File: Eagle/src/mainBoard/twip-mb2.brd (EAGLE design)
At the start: 82.2 x 82.5 mm, 19 parts, among them U1 GY-521MPU6050

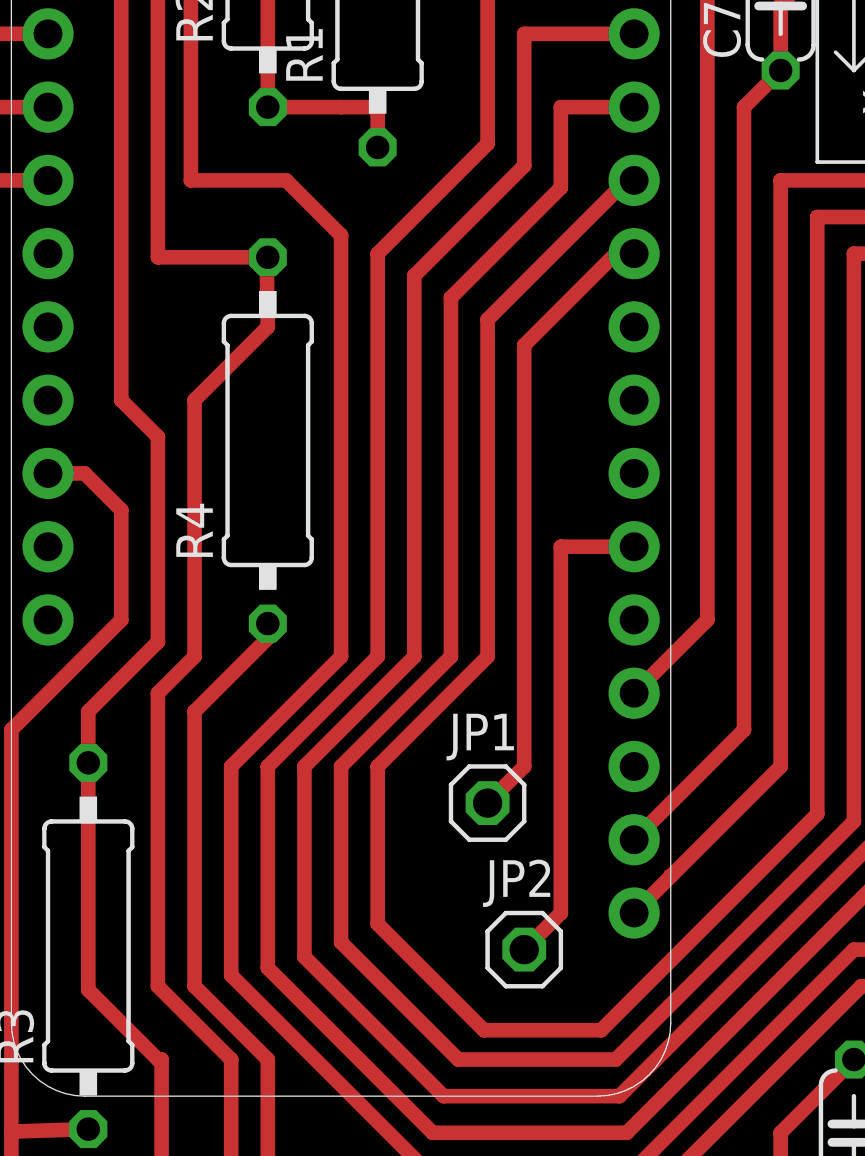
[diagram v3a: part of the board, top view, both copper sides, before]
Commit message: Update twip-mb2.brd
 mosfet pullup changes
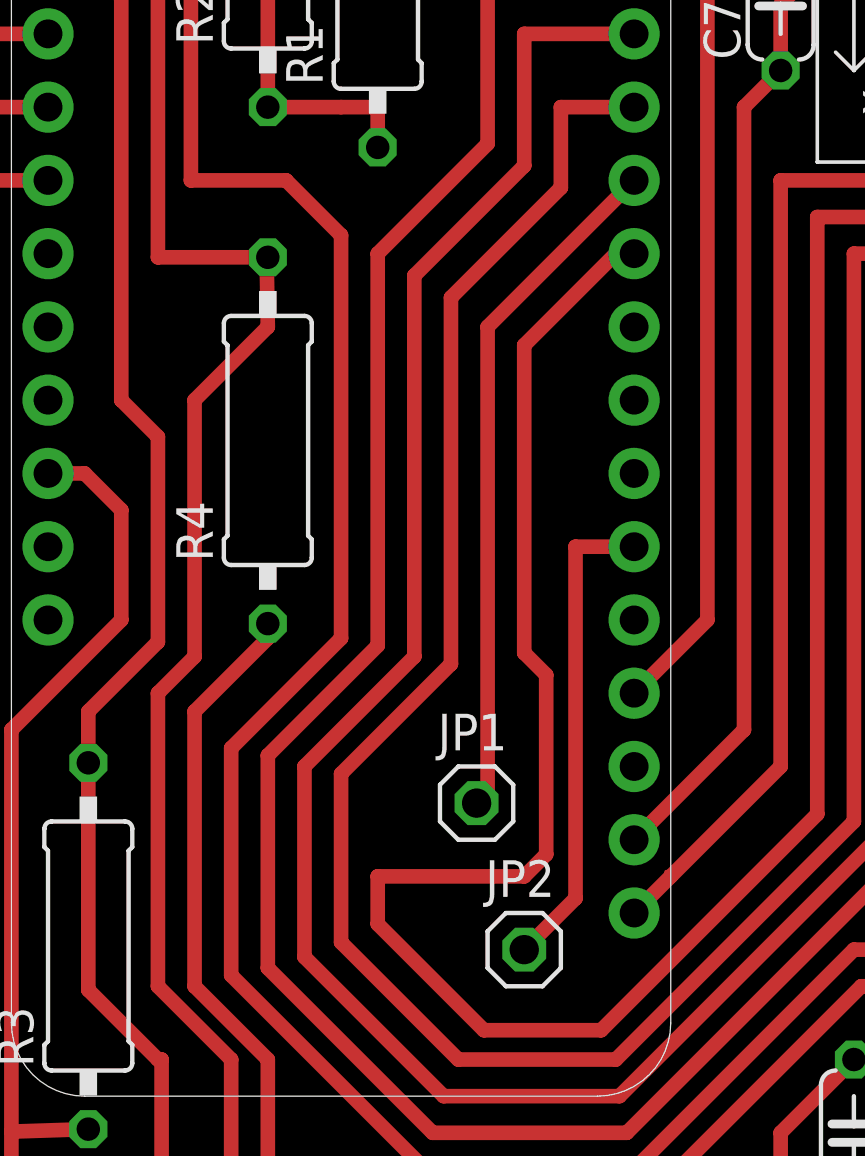
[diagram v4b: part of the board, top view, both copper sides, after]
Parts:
- moved JP1 0.38 mm to (25.0, 39.4)
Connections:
- net N$31: now also STEPDRV1.1; no longer JP1.1
- net N$32: now also JP1.1; no longer STEPDRV1.1
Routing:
- net N$31: track 21.5 -> 158.8 mm
- net N$32: track 157.5 -> 23.9 mm
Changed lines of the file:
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@@
 <attribute name="VALUE" x="64.897" y="68.961" size="1.27" layer="27" ratio="10" rot="R90"/>
 </element>
-<element name="JP1" library="pinhead" library_urn="urn:adsk.eagle:library:325" package="1X01" package3d_urn="urn:adsk.eagle:package:22485/2" value="" x="25.4" y="39.37" smashed="yes">
-<attribute name="NAME" x="24.0538" y="41.1988" size="1.27" layer="25" ratio="10"/>
-<attribute name="VALUE" x="24.13" y="36.195" size="1.27" layer="27"/>
+<element name="JP1" library="pinhead" library_urn="urn:adsk.eagle:library:325" package="1X01" package3d_urn="urn:adsk.eagle:package:22485/2" value="" x="25.019" y="39.37" smashed="yes">
+<attribute name="NAME" x="23.6728" y="41.1988" size="1.27" layer="25" ratio="10"/>
+<attribute name="VALUE" x="23.749" y="36.195" size="1.27" layer="27"/>
 </element>
 <element name="JP2" library="pinhead" library_urn="urn:adsk.eagle:library:325" package="1X01" package3d_urn="urn:adsk.eagle:package:22485/2" value="" x="26.67" y="34.29" smashed="yes">
@@
 <wire x1="20.32" y1="34.544" x2="24.384" y2="30.48" width="0.508" layer="1"/>
 <wire x1="74.93" y1="48.26" x2="64.77" y2="58.42" width="0.508" layer="1"/>
-<wire x1="20.32" y1="40.64" x2="20.32" y2="34.544" width="0.508" layer="1"/>
-<wire x1="20.32" y1="40.64" x2="24.13" y2="44.45" width="0.508" layer="1"/>
+<wire x1="20.32" y1="40.386" x2="20.32" y2="34.544" width="0.508" layer="1"/>
+<wire x1="20.32" y1="40.386" x2="24.13" y2="44.196" width="0.508" layer="1"/>
 <wire x1="24.384" y1="30.48" x2="29.845" y2="30.48" width="0.508" layer="1"/>
 <wire x1="29.845" y1="30.48" x2="38.1" y2="38.735" width="0.508" layer="1"/>
-<wire x1="24.13" y1="44.45" x2="24.13" y2="56.896" width="0.508" layer="1"/>
+<wire x1="24.13" y1="44.196" x2="24.13" y2="56.896" width="0.508" layer="1"/>
 <wire x1="27.94" y1="63.5" x2="30.48" y2="63.5" width="0.508" layer="1"/>
 <wire x1="24.13" y1="56.896" x2="27.94" y2="60.706" width="0.508" layer="1"/>
@@
 <wire x1="16.51" y1="33.401" x2="23.241" y2="26.67" width="0.508" layer="1"/>
 <wire x1="30.48" y1="26.67" x2="23.241" y2="26.67" width="0.508" layer="1"/>
-<wire x1="16.51" y1="40.64" x2="20.32" y2="44.45" width="0.508" layer="1"/>
-<wire x1="16.51" y1="40.64" x2="16.51" y2="33.401" width="0.508" layer="1"/>
-<wire x1="20.32" y1="44.45" x2="20.32" y2="59.055" width="0.508" layer="1"/>
+<wire x1="16.51" y1="41.275" x2="20.32" y2="45.085" width="0.508" layer="1"/>
+<wire x1="16.51" y1="41.275" x2="16.51" y2="33.401" width="0.508" layer="1"/>
+<wire x1="20.32" y1="45.085" x2="20.32" y2="59.055" width="0.508" layer="1"/>
 <wire x1="43.2562" y1="34.29" x2="44.2976" y2="33.2486" width="0.508" layer="1"/>
 <wire x1="38.1" y1="34.29" x2="43.2562" y2="34.29" width="0.508" layer="1"/>
@@
 <wire x1="33.02" y1="5.08" x2="30.48" y2="7.62" width="0.508" layer="1"/>
 </signal>
-<signal name="N$32">
-<contactref element="STEPDRV1" pad="1"/>
-<contactref element="MS2" pad="11"/>
-<wire x1="72.39" y1="8.89" x2="74.93" y2="8.89" width="0.508" layer="1"/>
-<wire x1="74.93" y1="8.89" x2="76.2" y2="10.16" width="0.508" layer="1"/>
-<wire x1="76.2" y1="10.16" x2="76.2" y2="49.53" width="0.508" layer="1"/>
-<wire x1="76.2" y1="49.53" x2="66.04" y2="59.69" width="0.508" layer="1"/>
-<wire x1="36.83" y1="59.69" x2="36.83" y2="38.989" width="0.508" layer="1"/>
-<wire x1="36.83" y1="38.989" x2="29.337" y2="31.496" width="0.508" layer="1"/>
-<wire x1="66.04" y1="59.69" x2="36.83" y2="59.69" width="0.508" layer="1"/>
-<wire x1="25.273" y1="31.496" x2="21.59" y2="35.179" width="0.508" layer="1"/>
-<wire x1="21.59" y1="35.179" x2="21.59" y2="40.64" width="0.508" layer="1"/>
-<wire x1="21.59" y1="40.64" x2="25.4" y2="44.45" width="0.508" layer="1"/>
-<wire x1="29.337" y1="31.496" x2="25.273" y2="31.496" width="0.508" layer="1"/>
-<wire x1="25.4" y1="44.45" x2="25.4" y2="56.134" width="0.508" layer="1"/>
-<wire x1="25.4" y1="56.134" x2="30.226" y2="60.96" width="0.508" layer="1"/>
-<wire x1="30.226" y1="60.96" x2="30.48" y2="60.96" width="0.508" layer="1"/>
-</signal>
 <signal name="N$34">
 <contactref element="STEPDRV2" pad="1"/>
@@
 <wire x1="30.226" y1="27.94" x2="23.495" y2="27.94" width="0.508" layer="1"/>
 <wire x1="23.495" y1="27.94" x2="17.78" y2="33.655" width="0.508" layer="1"/>
-<wire x1="17.78" y1="33.655" x2="17.78" y2="40.64" width="0.508" layer="1"/>
-<wire x1="21.59" y1="44.45" x2="17.78" y2="40.64" width="0.508" layer="1"/>
+<wire x1="17.78" y1="33.655" x2="17.78" y2="41.021" width="0.508" layer="1"/>
+<wire x1="21.59" y1="44.831" x2="17.78" y2="41.021" width="0.508" layer="1"/>
 <wire x1="25.4" y1="62.23" x2="25.4" y2="68.58" width="0.508" layer="1"/>
 <wire x1="25.4" y1="68.58" x2="30.48" y2="68.58" width="0.508" layer="1"/>
-<wire x1="21.59" y1="44.45" x2="21.59" y2="58.42" width="0.508" layer="1"/>
+<wire x1="21.59" y1="44.831" x2="21.59" y2="58.42" width="0.508" layer="1"/>
 <wire x1="25.4" y1="62.23" x2="21.59" y2="58.42" width="0.508" layer="1"/>
 <contactref element="IBC" pad="25"/>
@@
 <contactref element="MS2" pad="6"/>
 <contactref element="JP2" pad="1"/>
-<wire x1="30.48" y1="48.26" x2="27.94" y2="48.26" width="0.508" layer="1"/>
-<wire x1="27.94" y1="48.26" x2="27.94" y2="35.56" width="0.508" layer="1"/>
-<wire x1="27.94" y1="35.56" x2="26.67" y2="34.29" width="0.508" layer="1"/>
+<wire x1="30.48" y1="48.26" x2="28.448" y2="48.26" width="0.508" layer="1"/>
+<wire x1="28.448" y1="48.26" x2="28.448" y2="36.068" width="0.508" layer="1"/>
+<wire x1="28.448" y1="36.068" x2="26.67" y2="34.29" width="0.508" layer="1"/>
 </signal>
 <signal name="N$31">
 <contactref element="MS2" pad="10"/>
-<contactref element="JP1" pad="1"/>
-<wire x1="25.4" y1="39.37" x2="26.67" y2="40.64" width="0.508" layer="1"/>
-<wire x1="26.67" y1="40.64" x2="26.67" y2="55.245" width="0.508" layer="1"/>
+<wire x1="26.67" y1="44.577" x2="26.67" y2="55.245" width="0.508" layer="1"/>
 <wire x1="26.67" y1="55.245" x2="29.845" y2="58.42" width="0.508" layer="1"/>
 <wire x1="29.845" y1="58.42" x2="30.48" y2="58.42" width="0.508" layer="1"/>
+<contactref element="STEPDRV1" pad="1"/>
+<wire x1="72.39" y1="8.89" x2="74.93" y2="8.89" width="0.508" layer="1"/>
+<wire x1="74.93" y1="8.89" x2="76.2" y2="10.16" width="0.508" layer="1"/>
+<wire x1="76.2" y1="10.16" x2="76.2" y2="49.53" width="0.508" layer="1"/>
+<wire x1="76.2" y1="49.53" x2="66.04" y2="59.69" width="0.508" layer="1"/>
+<wire x1="36.83" y1="59.69" x2="36.83" y2="38.989" width="0.508" layer="1"/>
+<wire x1="36.83" y1="38.989" x2="29.337" y2="31.496" width="0.508" layer="1"/>
+<wire x1="66.04" y1="59.69" x2="36.83" y2="59.69" width="0.508" layer="1"/>
+<wire x1="25.273" y1="31.496" x2="21.59" y2="35.179" width="0.508" layer="1"/>
+<wire x1="21.59" y1="35.179" x2="21.59" y2="36.83" width="0.508" layer="1"/>
+<wire x1="29.337" y1="31.496" x2="25.273" y2="31.496" width="0.508" layer="1"/>
+<wire x1="26.67" y1="44.577" x2="27.432" y2="43.815" width="0.508" layer="1"/>
+<wire x1="27.432" y1="43.815" x2="27.432" y2="37.592" width="0.508" layer="1"/>
+<wire x1="27.432" y1="37.592" x2="26.67" y2="36.83" width="0.508" layer="1"/>
+<wire x1="26.67" y1="36.83" x2="21.59" y2="36.83" width="0.508" layer="1"/>
 </signal>
 <signal name="N$37">
@@
 <wire x1="54.864" y1="44.704" x2="57.15" y2="46.99" width="0.508" layer="1"/>
 </signal>
+<signal name="N$32">
+<contactref element="MS2" pad="11"/>
+<contactref element="JP1" pad="1"/>
+<wire x1="30.48" y1="60.96" x2="25.4" y2="55.88" width="0.508" layer="1"/>
+<wire x1="25.4" y1="39.751" x2="25.019" y2="39.37" width="0.508" layer="1"/>
+<wire x1="25.4" y1="55.88" x2="25.4" y2="39.751" width="0.508" layer="1"/>
+</signal>
 </signals>

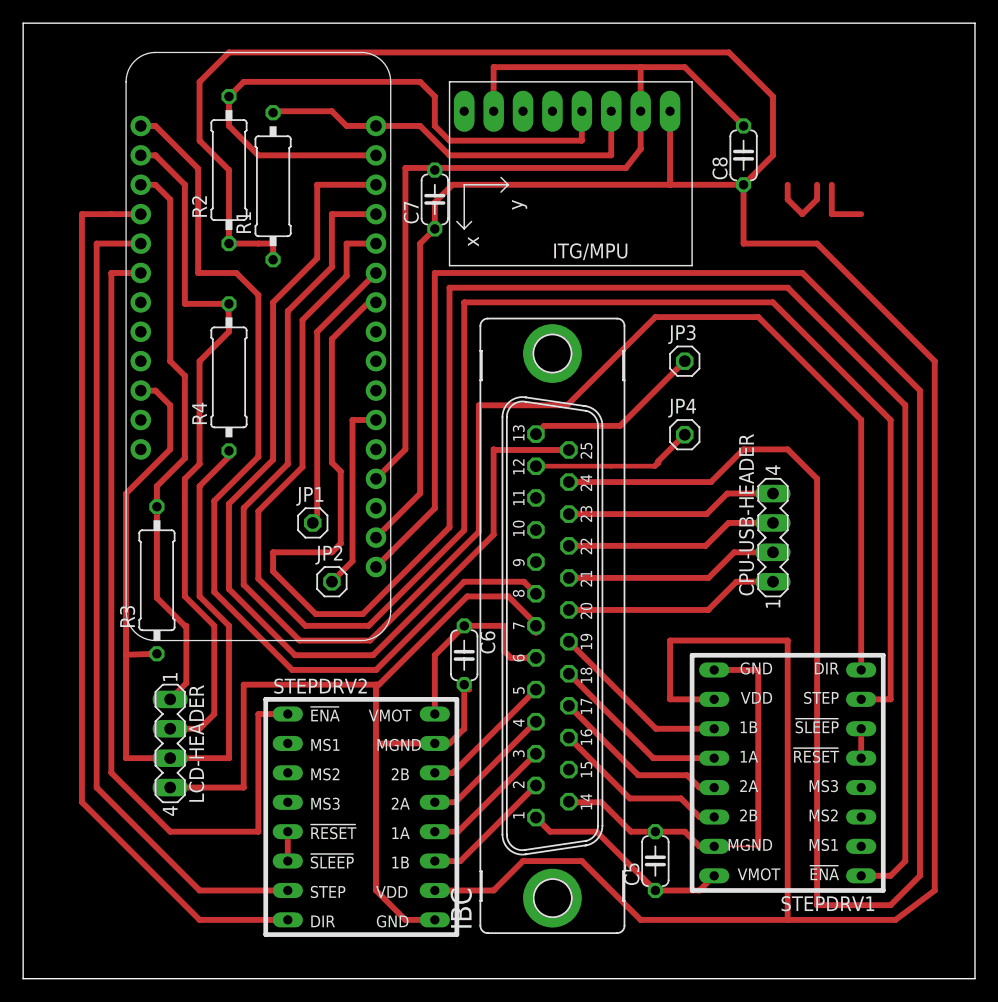
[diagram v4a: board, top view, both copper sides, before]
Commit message: Update twip-mb2.brd
big changes to  IBC pinouts  to  shift stepper connectors around
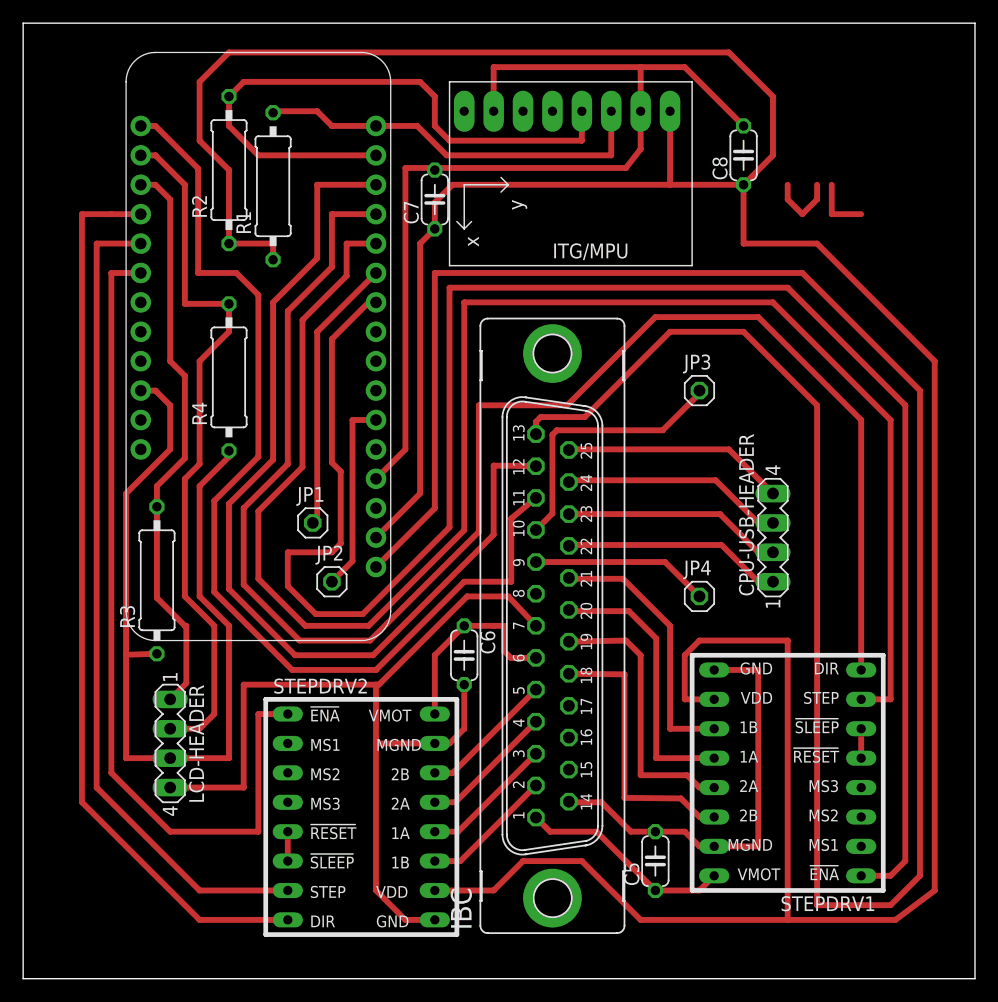
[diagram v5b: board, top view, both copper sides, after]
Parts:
- moved JP4 14.0 mm to (58.4, 33.0)
- moved JP3 2.84 mm to (58.4, 50.8)
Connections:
- net N$13: now also IBC.25; no longer IBC.23
- net N$14: now also IBC.24; no longer IBC.22
- net N$16: now also IBC.13; no longer IBC.24
- net N$18: now also IBC.23; no longer IBC.21
- net N$19: now also IBC.12; no longer IBC.25
- net N$28: now also IBC.11; no longer IBC.8
- net N$3: now also IBC.18; no longer IBC.16
- net N$30: now also IBC.22; no longer IBC.20
- net N$37: now also IBC.10; no longer IBC.13
- net N$38: now also IBC.9; no longer IBC.12
- net N$4: now also IBC.19; no longer IBC.17
- net N$6: now also IBC.20; no longer IBC.18
- net N$7: now also IBC.21; no longer IBC.19
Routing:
- net N$16: track 186.2 -> 199.9 mm
- net N$3: track 15.4 -> 23.9 mm
- net N$4: track 15.5 -> 23.9 mm
- net N$6: track 15.6 -> 23.9 mm
- net N$37: track 15.5 -> 23.2 mm
- net N$7: track 15.7 -> 23.2 mm
- net N$28: track 82.9 -> 88.6 mm
- net N$19: track 86.6 -> 82.3 mm
- net 3V: track 307.8 -> 304.4 mm
- net N$17: track 37.3 -> 34.7 mm
- net N$31: track 158.8 -> 157.0 mm
- net N$33: track 82.4 -> 80.6 mm
- net N$38: track 14.1 -> 15.4 mm
- net N$13: track 18.4 -> 19.2 mm
- net N$14: track 18.4 -> 19.2 mm

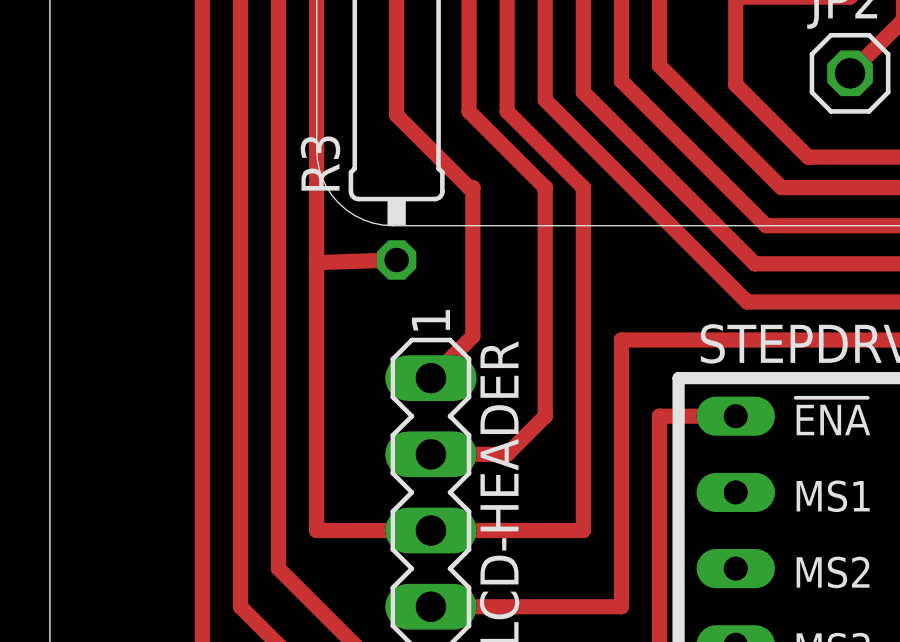
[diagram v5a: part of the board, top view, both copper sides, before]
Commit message: Update twip-mb2.brd
change LCD I2C wiring
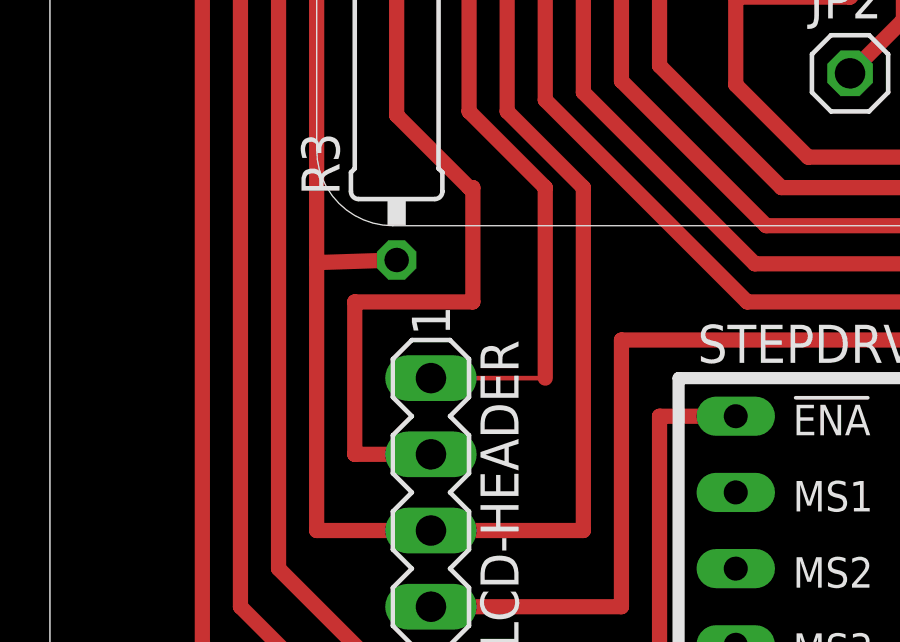
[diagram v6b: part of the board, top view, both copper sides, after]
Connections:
- net N$11: now also LCD-HEADER.2; no longer LCD-HEADER.1
- net N$35: now also LCD-HEADER.1; no longer LCD-HEADER.2
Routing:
- net N$11: track 49.5 -> 57.9 mm
- net N$35: track 61.4 -> 59.6 mm
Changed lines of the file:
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@@
 <signal name="N$11">
 <wire x1="13.97" y1="44.958" x2="13.97" y2="52.07" width="0.508" layer="1"/>
-<contactref element="LCD-HEADER" pad="1"/>
 <contactref element="R3" pad="2"/>
 <wire x1="13.97" y1="44.958" x2="11.557" y2="42.545" width="0.508" layer="1"/>
 <wire x1="11.557" y1="42.545" x2="11.557" y2="40.767" width="0.508" layer="1"/>
-<wire x1="14.097" y1="30.48" x2="14.097" y2="25.527" width="0.508" layer="1"/>
-<wire x1="12.7" y1="24.13" x2="14.097" y2="25.527" width="0.508" layer="1"/>
+<wire x1="14.097" y1="30.48" x2="14.097" y2="26.67" width="0.508" layer="1"/>
 <wire x1="11.557" y1="40.767" x2="11.557" y2="32.893" width="0.508" layer="1"/>
 <wire x1="11.557" y1="32.893" x2="13.97" y2="30.48" width="0.508" layer="1"/>
@@
 <wire x1="13.97" y1="52.07" x2="12.7" y2="53.34" width="0.508" layer="1"/>
 <wire x1="12.7" y1="53.34" x2="12.7" y2="67.31" width="0.508" layer="1"/>
+<wire x1="14.097" y1="26.67" x2="10.16" y2="26.67" width="0.508" layer="1"/>
+<contactref element="LCD-HEADER" pad="2"/>
+<wire x1="10.16" y1="26.67" x2="10.16" y2="21.59" width="0.508" layer="1"/>
+<wire x1="10.16" y1="21.59" x2="12.7" y2="21.59" width="0.508" layer="1"/>
 </signal>
 <signal name="N$33">
@@
 <signal name="N$35">
 <contactref element="R4" pad="2"/>
-<contactref element="LCD-HEADER" pad="2"/>
-<wire x1="12.7" y1="21.59" x2="15.24" y2="21.59" width="0.508" layer="1"/>
-<wire x1="15.24" y1="21.59" x2="16.51" y2="22.86" width="0.508" layer="1"/>
-<wire x1="16.51" y1="30.48" x2="16.51" y2="22.86" width="0.508" layer="1"/>
+<wire x1="16.51" y1="30.48" x2="16.51" y2="24.13" width="0.508" layer="1"/>
 <wire x1="15.24" y1="53.34" x2="17.78" y2="55.88" width="0.508" layer="1"/>
 <wire x1="15.24" y1="53.34" x2="15.24" y2="44.45" width="0.508" layer="1"/>
@@
 <wire x1="13.97" y1="58.293" x2="17.78" y2="58.293" width="0.508" layer="1"/>
 <wire x1="17.78" y1="55.88" x2="17.78" y2="58.293" width="0.508" layer="1"/>
+<contactref element="LCD-HEADER" pad="1"/>
+<wire x1="12.7" y1="24.13" x2="16.51" y2="24.13" width="0.1524" layer="1"/>
 </signal>
 <signal name="N$19">
